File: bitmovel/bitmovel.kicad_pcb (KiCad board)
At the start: 2 copper layers, 90 x 80 mm, 20 parts, among them J1 Conn_01x02_Male, J2 micro:bit, J3 motor D, J4 motor E, SW1 SW_SPST, U1 LM1117-3.3, U2 L293D

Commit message: Atualizando URL e versão da placa impressas na silkscreen
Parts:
- added G***: LOGO, LOGO, F.Cu at (150.0, 114.5)
- moved G*** 5.00 mm to (150.0, 105.0)
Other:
- net class Default removed
- board text added: "https://escola4pontozero.fee.unicamp.br"
- board text added: "v2"
- board text removed: "Escola 4.0"
- board text removed: "www.escola4pontozero.com.br"

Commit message: Inclui ilhas para conectar P14, P16, 3V3 e GND
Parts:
- added J5: Conn_01x02_Female, Connector_PinHeader_2.54mm:PinHeader_1x02_P2.54mm_Vertical, F.Cu at (179.6, 80.3)
- added J6: Conn_01x02_Female, Connector_PinHeader_2.54mm:PinHeader_1x02_P2.54mm_Vertical, F.Cu at (179.6, 84.3)
- added J7: Conn_01x01_Female, Connector_PinHeader_2.54mm:PinHeader_1x01_P2.54mm_Vertical, F.Cu at (158.0, 59.7)
- added J8: Conn_01x01_Female, Connector_PinHeader_2.54mm:PinHeader_1x01_P2.54mm_Vertical, F.Cu at (153.7, 59.7)
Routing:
- net /3.3V: track 92.9 -> 104.8 mm
- net Net-(J2-Pad10): track 0.00 -> 5.59 mm
- net Net-(J2-Pad9): track 0.00 -> 5.53 mm

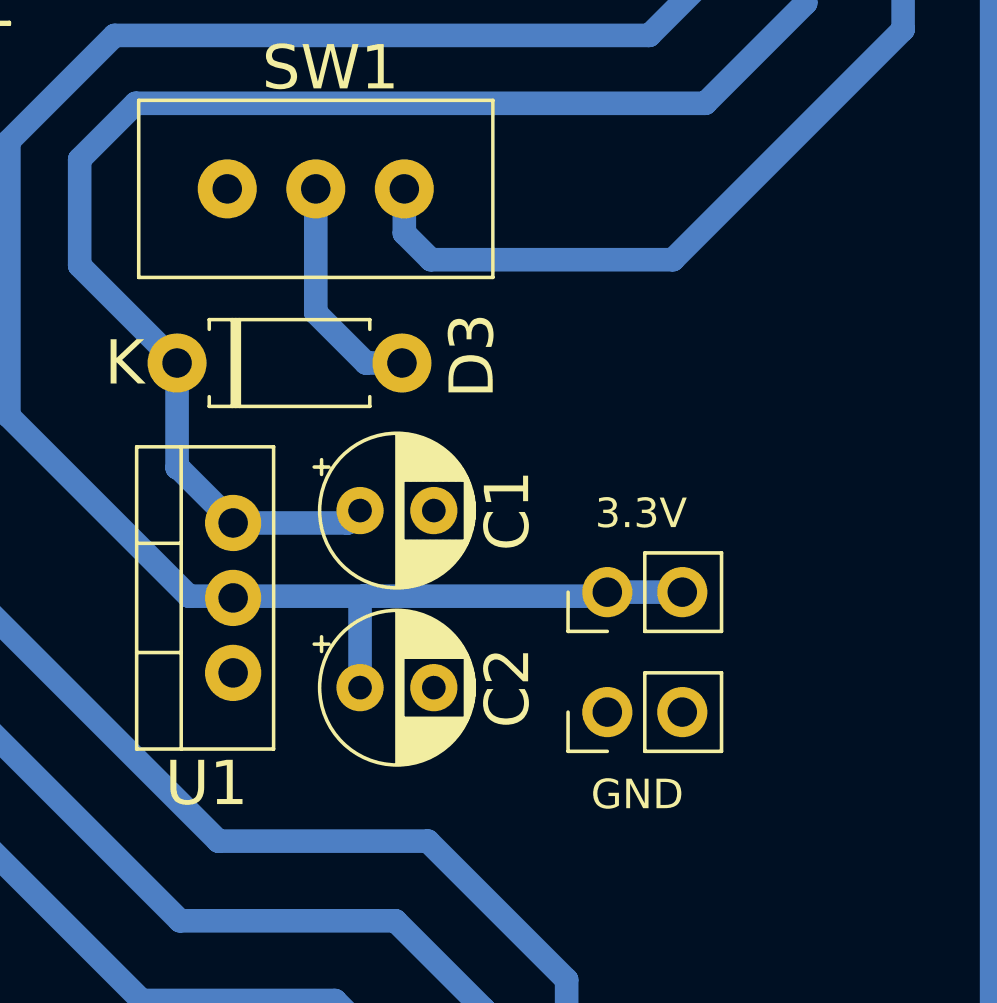
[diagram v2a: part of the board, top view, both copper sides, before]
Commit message: Inclui ilhas para conectar a Vin
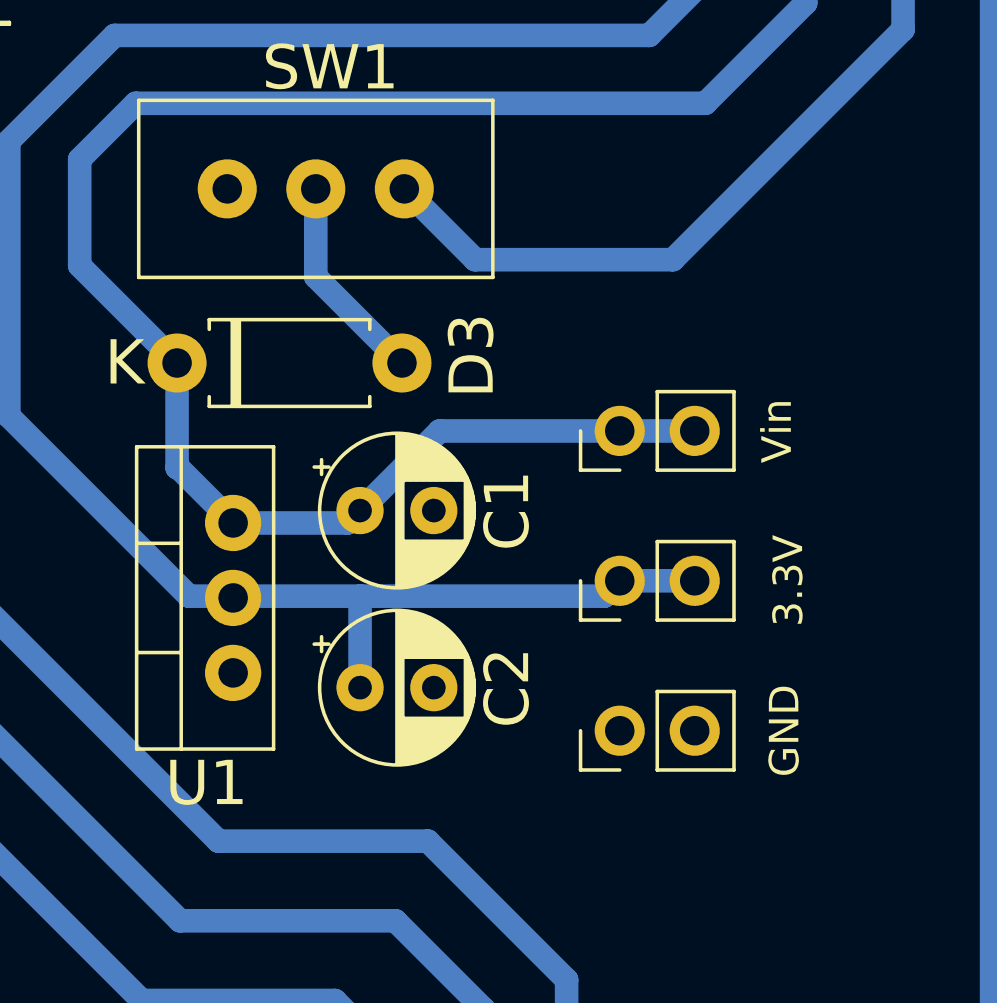
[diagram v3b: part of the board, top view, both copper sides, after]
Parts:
- added J9: Conn_01x02_Female, Connector_PinHeader_2.54mm:PinHeader_1x02_P2.54mm_Vertical, F.Cu at (180.0, 74.8)
- moved J6 0.76 mm to (180.0, 85.0)
- moved J5 0.57 mm to (180.0, 79.9)
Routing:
- net /Vin: track 279.8 -> 292.1 mm
- net Net-(J1-Pad2): track 27.1 -> 26.3 mm
- net Net-(D3-Pad2): track 7.62 -> 6.91 mm
- net /3.3V: track 104.8 -> 105.3 mm

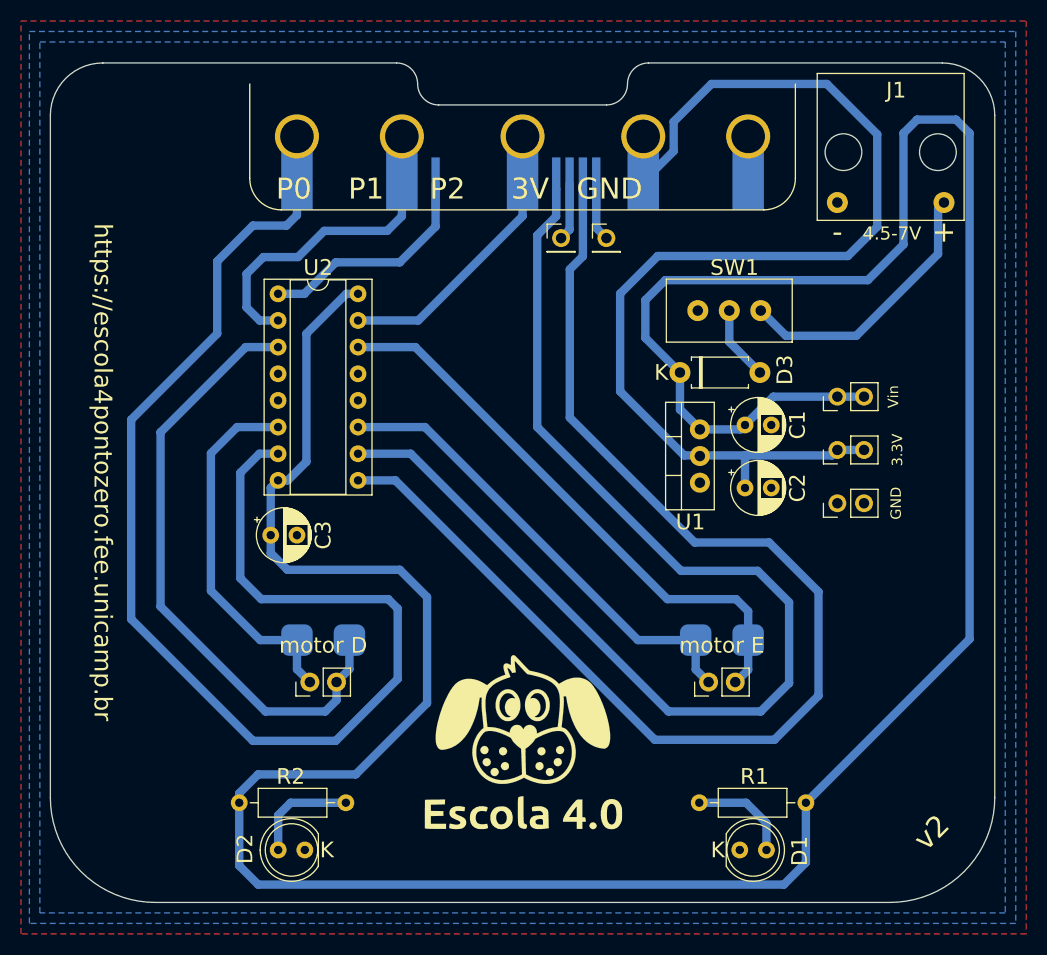
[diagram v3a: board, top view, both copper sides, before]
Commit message: Corrige posição das ilhas 3v3 e GND
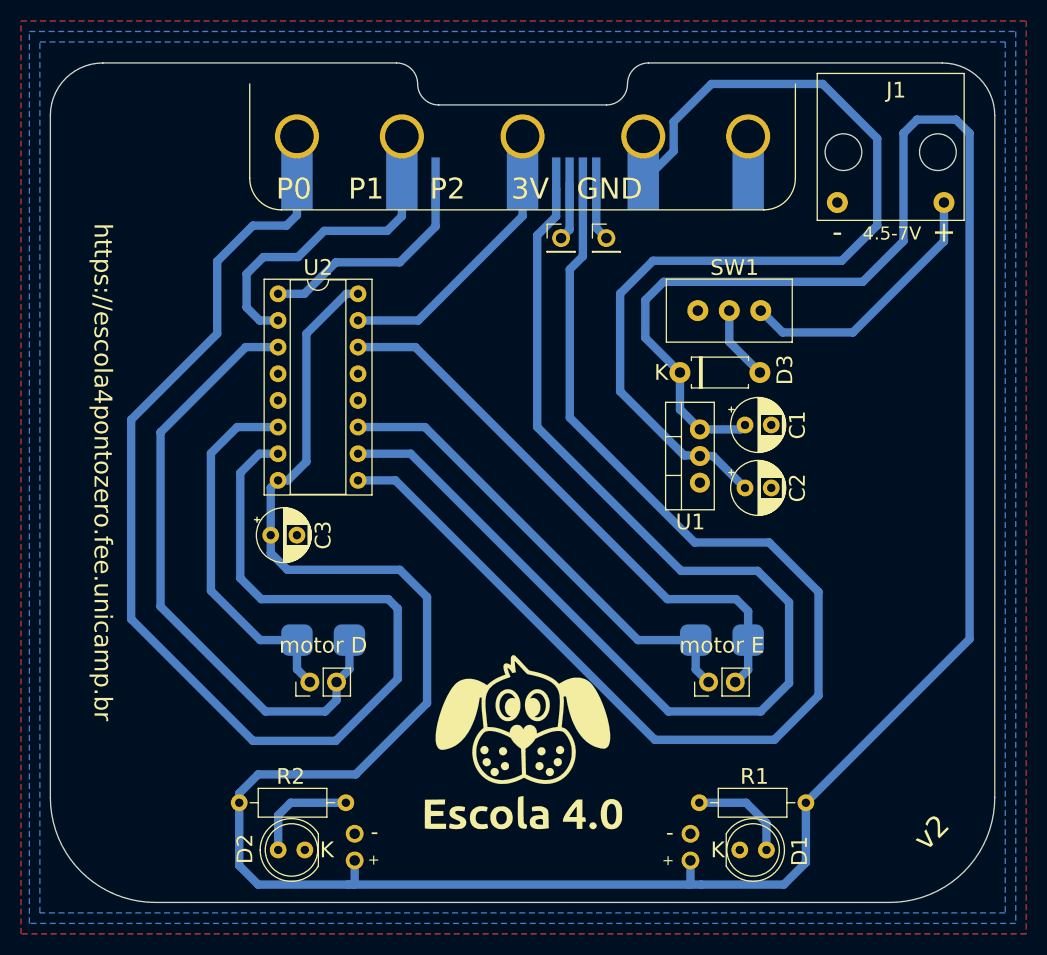
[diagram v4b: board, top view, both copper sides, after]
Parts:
- removed J5: Conn_01x02_Female, Connector_PinHeader_2.54mm:PinHeader_1x02_P2.54mm_Vertical
- moved J6 57.2 mm to (134.0, 119.0), turned to 180 degrees
- moved J9 46.4 mm to (166.0, 119.0), turned to 180 degrees
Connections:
- J6 pad 1: GND -> /Vin
- J9 pad 2: /Vin -> GND
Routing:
- net /3.3V: track 105.3 -> 91.6 mm
- net /Vin: track 292.1 -> 284.3 mm
- net Net-(J1-Pad2): track 26.3 -> 25.6 mm

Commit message: Atualiza gerbers
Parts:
- moved R2 1.00 mm to (123.0, 112.5)
- moved R1 1.00 mm to (177.0, 112.5)
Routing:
- net Net-(J2-Pad1): track 120.9 -> 120.1 mm
- net /Vin: track 284.3 -> 283.7 mm

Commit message: Atualiza versão para v3 e outros ajustes na silkscreen
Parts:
- moved G*** 2.00 mm to (150.0, 103.0)
- moved G*** 2.00 mm to (150.0, 112.5)
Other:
- board text added: "v3"
- board text removed: "v2"
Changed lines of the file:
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@@
   )
   (footprint "Personal:logo_escola" (layer "F.Cu")
-    (at 150 105)
+    (at 150 103)
     (attr through_hole)
     (fp_text reference "G***" (at 0 0) (layer "F.SilkS") hide
@@
       (effects (font (size 1 1) (thickness 0.15)))
     )
-    (fp_text user "K" (at -1.78 0) (layer "F.SilkS")
+    (fp_text user "k" (at -1.78 0) (layer "F.SilkS")
       (effects (font (size 1.5 1.5) (thickness 0.2)))
     )
@@
     (pad "2" thru_hole circle locked (at 10.16 0 90) (size 2 2) (drill 1) (layers *.Cu *.Mask)
       (net 17 "Net-(J1-Pad2)") (pinfunction "Pin_2") (pintype "passive"))
-    (model "C:/Users/Samuel/Google Drive/Escola40/modelos 3D/USB-5pin-board.step"
+    (model "${KIPRJMOD}/3Dmodels/USB-5pin-board.step"
       (offset (xyz 5 5.5 0))
       (scale (xyz 1 1 1))
@@
       (effects (font (size 1 1) (thickness 0.15)))
     )
-    (fp_text user "K" (at -2.1 0) (layer "F.SilkS")
+    (fp_text user "k" (at -2.1 0) (layer "F.SilkS")
       (effects (font (size 1.5 1.5) (thickness 0.2)))
     )
@@
       (effects (font (size 1 1) (thickness 0.15)))
     )
-    (fp_text user "K" (at -2.1 0) (layer "F.SilkS")
+    (fp_text user "k" (at -2.1 0) (layer "F.SilkS")
       (effects (font (size 1.5 1.5) (thickness 0.2)))
     )
@@
   )
   (footprint "LOGO" (layer "F.Cu")
-    (at 150 114.5)
+    (at 150 112.5)
     (attr board_only exclude_from_pos_files exclude_from_bom)
     (fp_text reference "G***" (at 0 0) (layer "F.SilkS") hide
@@
       (effects (font (size 1 1) (thickness 0.15)))
     )
-    (fp_text user "+" (at -1.8138 0.001 180 unlocked) (layer "F.SilkS")
-      (effects (font (size 1 1) (thickness 0.15)))
-    )
-    (fp_text user "-" (at -1.89 2.4648 180 unlocked) (layer "F.SilkS")
+    (fp_text user "+" (at -2 0.001 180 unlocked) (layer "F.SilkS")
+      (effects (font (size 1.5 1.5) (thickness 0.2)))
+    )
+    (fp_text user "-" (at -2 2.4648 180 unlocked) (layer "F.SilkS")
       (effects (font (size 1.5 1.5) (thickness 0.2)))
     )
@@
     (fp_text value "Conn_01x01_Female" (at 0 2.33) (layer "F.Fab")
       (effects (font (size 1 1) (thickness 0.15)))
+    )
+    (fp_text user "IR_E" (at 0 5.31 90 unlocked) (layer "F.SilkS")
+      (effects (font (size 1.5 1.5) (thickness 0.2)))
     )
     (fp_text user "${REFERENCE}" (at 0 0 90) (layer "F.Fab")
@@
       (effects (font (size 1 1) (thickness 0.15)))
     )
-    (fp_text user "-" (at 1.9668 2.668 unlocked) (layer "F.SilkS")
+    (fp_text user "-" (at 2 2.668 unlocked) (layer "F.SilkS")
       (effects (font (size 1.5 1.5) (thickness 0.2)))
     )
-    (fp_text user "+" (at 2.17 -0.0244 90 unlocked) (layer "F.SilkS")
-      (effects (font (size 1 1) (thickness 0.15)))
+    (fp_text user "+" (at 2 -0.0244 90 unlocked) (layer "F.SilkS")
+      (effects (font (size 1.5 1.5) (thickness 0.2)))
     )
     (fp_text user "${REFERENCE}" (at 0 1.27 90) (layer "F.Fab")
@@
     (fp_text value "Conn_01x01_Female" (at 0 2.33) (layer "F.Fab")
       (effects (font (size 1 1) (thickness 0.15)))
+    )
+    (fp_text user "IR_D" (at 0 5.31 90 unlocked) (layer "F.SilkS")
+      (effects (font (size 1.5 1.5) (thickness 0.2)))
     )
     (fp_text user "${REFERENCE}" (at 0 0 90) (layer "F.Fab")
@@
     (effects (font (size 1.7 1.7) (thickness 0.2)))
   )
-  (gr_text "v2" (at 188.976 116.332 45) (layer "F.SilkS")
+  (gr_text "v3" (at 188.976 116.332 45) (layer "F.SilkS")
     (effects (font (size 2 2) (thickness 0.2)))
   )
